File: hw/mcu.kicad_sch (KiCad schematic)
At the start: 38 parts, among them J6 SWD, U4 STM32G474CEU6, Y1 16MHz 9pF

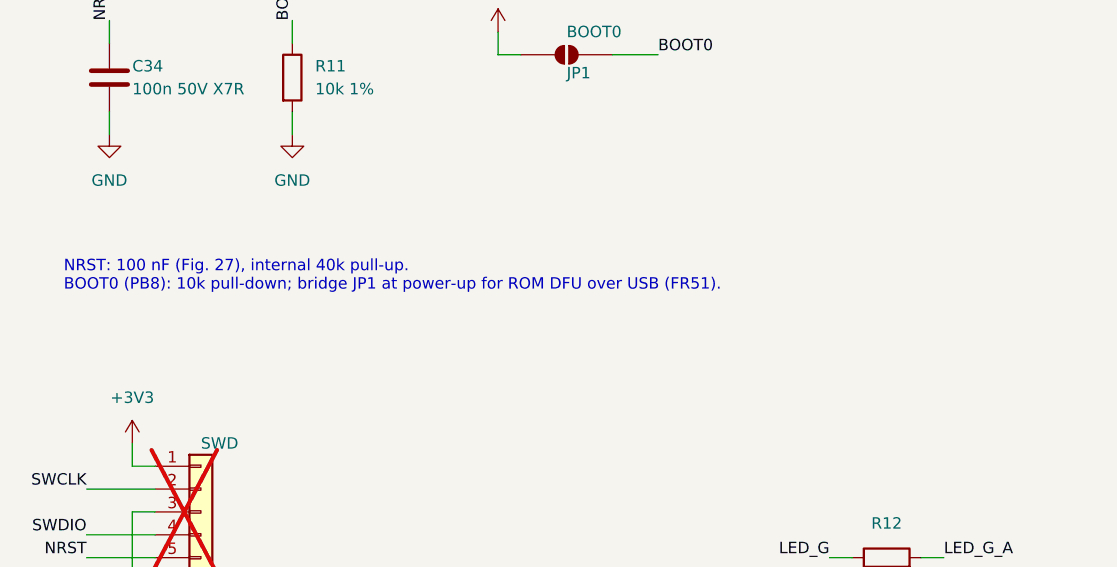
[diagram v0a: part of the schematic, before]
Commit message: Remove requirement IDs from schematic notes
Notes now state the reason in plain words so the schematic reads
without the requirements document.

Co-Authored-By: Claude Opus 5.5 <noreply@anthropic.com>
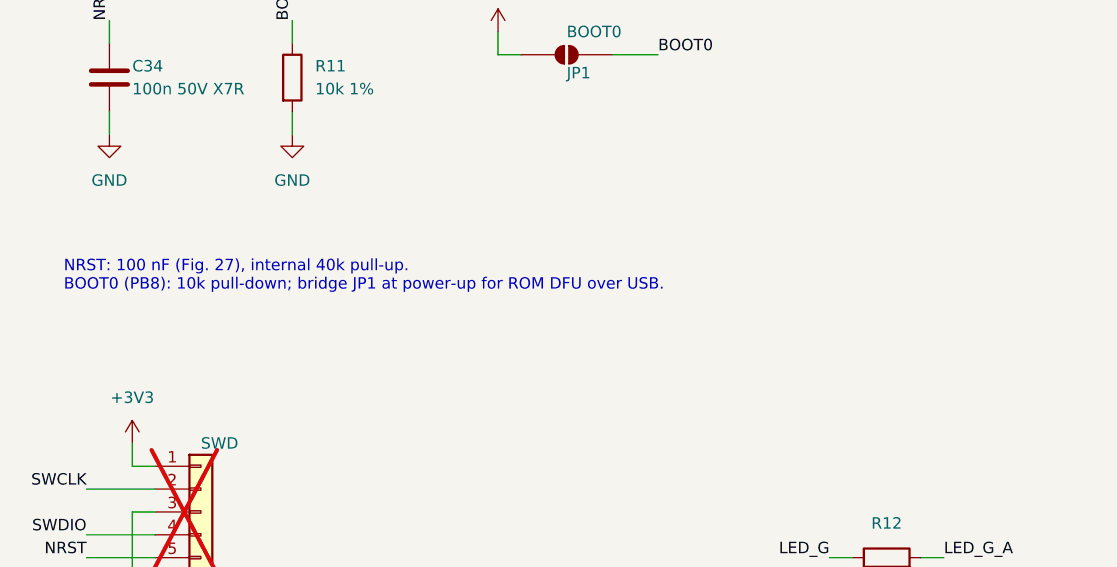
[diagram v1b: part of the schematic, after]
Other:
- note added: "NRST: 100 nF (Fig. 27), internal 40k pull-up. BOOT0 (PB8): 10k pull-down; bridge JP1 at power-up for ROM DFU over USB."
- note removed: "NRST: 100 nF (Fig. 27), internal 40k pull-up. BOOT0 (PB8): 10k pull-down; bridge JP1 at power-up for ROM DFU over USB (FR51)."
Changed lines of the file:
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@@
 		)
 	)
-	(text "NRST: 100 nF (Fig. 27), internal 40k pull-up.\nBOOT0 (PB8): 10k pull-down; bridge JP1 at power-up for ROM DFU over USB (FR51)."
+	(text "NRST: 100 nF (Fig. 27), internal 40k pull-up.\nBOOT0 (PB8): 10k pull-down; bridge JP1 at power-up for ROM DFU over USB."
 		(exclude_from_sim no)
 		(at 25.4 172.72 0.0000)

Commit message: Place the 45 x 45 mm two-sided board and review its risks
Ceramic-only bulk caps, per-phase caps under each FET pair, one FET row,
corner M3 holes, USB-C and CAN on the motor side, XT30s closer together.
Encoder clearance 10 mm, 10 A RMS rating with no heatsink. Placement
fixes from the risk review: BOOT0 pad away from VBUS, 3 mm clear around
the XT30 power joints, edge caps parallel to the edge. Specs, layout
check and risk review updated; fuse and regen clamp now required
off-board parts.

Co-Authored-By: Claude Opus 5.5 <noreply@anthropic.com>
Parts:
- removed TP1: TP_3V3, TestPoint:TestPoint_Pad_D1.0mm, symbol Connector:TestPoint
- removed TP2: TP_5V, TestPoint:TestPoint_Pad_D1.0mm, symbol Connector:TestPoint
- removed TP3: TP_VBUS, TestPoint:TestPoint_Pad_D1.0mm, symbol Connector:TestPoint
- removed TP5: TP_SOA, TestPoint:TestPoint_Pad_D1.0mm, symbol Connector:TestPoint
- removed TP6: TP_SOB, TestPoint:TestPoint_Pad_D1.0mm, symbol Connector:TestPoint
- removed TP7: TP_SOC, TestPoint:TestPoint_Pad_D1.0mm, symbol Connector:TestPoint
- removed TP8: TP_DRV_nFAULT, TestPoint:TestPoint_Pad_D1.0mm, symbol Connector:TestPoint

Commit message: Route the 6-layer board and finalize parts for ordering
The 45 x 45 mm board is fully routed on six layers (F / GND / SIG /
SIG / PWR / B, 2 oz outer, 1 oz inner): DRC 0 errors, 0 unconnected,
schematic parity 0. Four layers could not route the DRV-to-MCU links
without moving the power or input stage.

- Encoder shares the DRV8353's SPI3 bus, as on the PoC; PA5-PA7 are
  unused. R25 pulls DRV nSCS up, since the DRV's logic inputs have an
  internal pull-down. The SDO / MISO pin-type warning is an ERC
  exclusion with a note.
- MCU is now the STM32G473CEU6: the G474 without the unused HRTIM,
  checked pin for pin against both datasheets, in stock and cheaper.
- Male XT30PW-M power connectors, HCS1206 shunts, SWD pads at the
  board edge.
- Design doc and review notes updated for the new stack-up, shared
  bus and MCU.

Co-Authored-By: Claude Opus 5.5 <noreply@anthropic.com>
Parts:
- J6: footprint Connector_PinHeader_2.54mm:PinHeader_1x05_P2.54mm_Vertical -> foc_controller:SWD_Pads_1x05_P1.27mm_SMD
- U4: value STM32G474CEU6 -> STM32G473CEU6; symbol MCU_ST_STM32G4:STM32G474CEUx -> MCU_ST_STM32G4:STM32G473CEUx; LCSC C1235412 -> C1342773; MPN STM32G474CEU6 -> STM32G473CEU6
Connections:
- net ENC_MISO is gone; now on net DRV_SDO: U4.40 (PC11)
- net ENC_MOSI is gone; now on net DRV_SDI: U4.43 (PB5)
- net ENC_SCK is gone; now on net DRV_SCLK: U4.39 (PC10)
- net CAN_TX: now also U4.42 (PB4); no longer U4.38 (PA15)
- net DRV_EN: now also U4.29 (PC6); no longer U4.24 (PB11)
- net DRV_SCLK: no longer U4.13 (PA5)
- net DRV_SDI: no longer U4.15 (PA7)
- net DRV_SDO: no longer U4.14 (PA6)
- net DRV_nFAULT: now also U4.44 (PB6); no longer U4.22 (PB10)
- net DRV_nSCS: now also U4.38 (PA15); no longer U4.45 (PB7)
- net ENC_CS: now also U4.24 (PB11); no longer U4.25 (PB12)
- net INHA: now also U4.32 (PA10); no longer U4.30 (PA8)
- net INHC: now also U4.30 (PA8); no longer U4.32 (PA10)
- net INLA: now also U4.28 (PB15); no longer U4.26 (PB13)
- net INLC: now also U4.26 (PB13); no longer U4.28 (PB15)
- no-connect marks 8 -> 11
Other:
- note added: "J6: 1.27 mm SMD pads for debugging only, Nucleo ST-LINK CN4 order (VDD, SWCLK, GND, SWDIO, NRST). Not fitted: solder wires or a 1.27 mm header if needed."
- note removed: "J6: 2.54 mm pads for debugging only, Nucleo ST-LINK CN4 order (VDD, SWCLK, GND, SWDIO, NRST). Not fitted: hand-solder a header if needed."
- title: MCU STM32G474 -> MCU STM32G473
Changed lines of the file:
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@@
 	(paper "A3")
 	(title_block
-		(title "MCU STM32G474")
+		(title "MCU STM32G473")
 		(date "2026-10-19")
 		(rev "A")
@@
 		)
 	)
-	(text "J6: 2.54 mm pads for debugging only, Nucleo ST-LINK CN4 order\n(VDD, SWCLK, GND, SWDIO, NRST). Not fitted: hand-solder a header if needed."
+	(text "J6: 1.27 mm SMD pads for debugging only, Nucleo ST-LINK CN4 order\n(VDD, SWCLK, GND, SWDIO, NRST). Not fitted: solder wires or a 1.27 mm header if needed."
 		(exclude_from_sim no)
 		(at 25.4 218.44 0)
@@
 	)
 	(no_connect
-		(at 187.96 149.86)
-	)
-	(no_connect
-		(at 187.96 154.94)
-	)
-	(no_connect
 		(at 187.96 134.62)
 	)
 	(no_connect
-		(at 187.96 121.92)
-	)
-	(no_connect
 		(at 187.96 119.38)
 	)
@@
 	(wire
 		(pts
-			(xy 187.96 165.1) (xy 180.34 165.1)
-		)
-		(stroke
-			(width 0)
-			(type default)
-		)
-	)
-	(wire
-		(pts
 			(xy 113.03 220.98) (xy 110.49 220.98)
 		)
@@
 	(wire
 		(pts
-			(xy 223.52 119.38) (xy 231.14 119.38)
-		)
-		(stroke
-			(width 0)
-			(type default)
-		)
-	)
-	(wire
-		(pts
 			(xy 76.2 44.45) (xy 76.2 46.99)
 		)
@@
 	(wire
 		(pts
-			(xy 223.52 116.84) (xy 231.14 116.84)
-		)
-		(stroke
-			(width 0)
-			(type default)
-		)
-	)
-	(wire
-		(pts
-			(xy 187.96 170.18) (xy 180.34 170.18)
-		)
-		(stroke
-			(width 0)
-			(type default)
-		)
-	)
-	(wire
-		(pts
 			(xy 121.92 44.45) (xy 121.92 46.99)
 		)
@@
 	(wire
 		(pts
-			(xy 187.96 157.48) (xy 180.34 157.48)
-		)
-		(stroke
-			(width 0)
-			(type default)
-		)
-	)
-	(wire
-		(pts
 			(xy 365.76 46.99) (xy 365.76 44.45)
 		)
@@
 	(wire
 		(pts
-			(xy 223.52 114.3) (xy 231.14 114.3)
-		)
-		(stroke
-			(width 0)
-			(type default)
-		)
-	)
-	(wire
-		(pts
 			(xy 223.52 121.92) (xy 231.14 121.92)
 		)
@@
 		)
 	)
-	(hierarchical_label "INHC"
+	(hierarchical_label "INHA"
 		(shape output)
 		(at 231.14 127 0)
@@
 		)
 	)
-	(hierarchical_label "DRV_SDO"
-		(shape input)
-		(at 231.14 116.84 0)
-		(effects
-			(font
-				(size 1.27 1.27)
-			)
-			(justify left)
-		)
-	)
-	(hierarchical_label "INHA"
+	(hierarchical_label "INHC"
 		(shape output)
 		(at 231.14 121.92 0)
@@
 		)
 	)
-	(hierarchical_label "ENC_CS"
-		(shape output)
-		(at 180.34 170.18 180)
-		(effects
-			(font
-				(size 1.27 1.27)
-			)
-			(justify right)
-		)
-	)
-	(hierarchical_label "ENC_MOSI"
+	(hierarchical_label "DRV_SDI"
 		(shape output)
 		(at 180.34 152.4 180)
@@
 		)
 	)
-	(hierarchical_label "DRV_SCLK"
-		(shape output)
-		(at 231.14 114.3 0)
-		(effects
-			(font
-				(size 1.27 1.27)
-			)
-			(justify left)
-		)
-	)
-	(hierarchical_label "INLC"
+	(hierarchical_label "INLA"
 		(shape output)
 		(at 180.34 177.8 180)
@@
 		)
 	)
-	(hierarchical_label "ENC_SCK"
+	(hierarchical_label "DRV_SCLK"
 		(shape output)
 		(at 180.34 124.46 180)
@@
 		)
 	)
-	(hierarchical_label "DRV_nFAULT"
-		(shape input)
-		(at 180.34 165.1 180)
-		(effects
-			(font
-				(size 1.27 1.27)
-			)
-			(justify right)
-		)
-	)
-	(hierarchical_label "DRV_SDI"
-		(shape output)
-		(at 231.14 119.38 0)
-		(effects
-			(font
-				(size 1.27 1.27)
-			)
-			(justify left)
-		)
-	)
-	(hierarchical_label "DRV_EN"
+	(hierarchical_label "ENC_CS"
 		(shape output)
 		(at 180.34 167.64 180)
@@
 		)
 	)
-	(hierarchical_label "CAN_TX"
+	(hierarchical_label "DRV_nSCS"
 		(shape output)
 		(at 231.14 139.7 0)
@@
 		)
 	)
-	(hierarchical_label "DRV_nSCS"
-		(shape output)
-		(at 180.34 157.48 180)
-		(effects
-			(font
-				(size 1.27 1.27)
-			)
-			(justify right)
-		)
-	)
 	(hierarchical_label "CAN_STB"
 		(shape output)
@@
 		)
 	)
-	(hierarchical_label "INLA"
+	(hierarchical_label "INLC"
 		(shape output)
 		(at 180.34 172.72 180)
@@
 		)
 	)
-	(hierarchical_label "ENC_MISO"
+	(hierarchical_label "DRV_SDO"
 		(shape input)
 		(at 180.34 127 180)
@@
 			)
 		)
-		(property "Footprint" "Connector_PinHeader_2.54mm:PinHeader_1x05_P2.54mm_Vertical"
+		(property "Footprint" "foc_controller:SWD_Pads_1x05_P1.27mm_SMD"
 			(at 40.64 200.66 0)
 			(hide yes)
@@
 	)
 	(symbol
-		(lib_id "MCU_ST_STM32G4:STM32G474CEUx")
+		(lib_id "MCU_ST_STM32G4:STM32G473CEUx")
 		(at 205.74 139.7 0)
 		(unit 1)
@@
 			)
 		)
-		(property "Value" "STM32G474CEU6"
+		(property "Value" "STM32G473CEU6"
 			(at 213.36 184.15 0)
 			(show_name no)
@@
 			)
 		)
-		(property "Datasheet" "https://www.st.com/resource/en/datasheet/stm32g474ce.pdf"
+		(property "Datasheet" "https://www.st.com/resource/en/datasheet/stm32g473ce.pdf"
 			(at 205.74 139.7 0)
 			(hide yes)
@@
 			)
 		)
-		(property "LCSC" "C1235412"
+		(property "LCSC" "C1342773"
 			(at 208.28 144.7799 0)
 			(hide yes)
@@
 			)
 		)
-		(property "MPN" "STM32G474CEU6"
+		(property "MPN" "STM32G473CEU6"
 			(at 208.28 144.7799 0)
 			(hide yes)
@@
 		)
 	)
+	(wire
+		(pts
+			(xy 180.34 149.86) (xy 187.96 149.86)
+		)
+		(stroke
+			(width 0)
+			(type default)
+		)
+	)
+	(hierarchical_label "CAN_TX"
+		(shape output)
+		(at 180.34 149.86 180)
+		(effects
+			(font
+				(size 1.27 1.27)
+			)
+			(justify right)
+		)
+	)
+	(wire
+		(pts
+			(xy 180.34 154.94) (xy 187.96 154.94)
+		)
+		(stroke
+			(width 0)
+			(type default)
+		)
+	)
+	(hierarchical_label "DRV_nFAULT"
+		(shape input)
+		(at 180.34 154.94 180)
+		(effects
+			(font
+				(size 1.27 1.27)
+			)
+			(justify right)
+		)
+	)
+	(no_connect
+		(at 187.96 157.48)
+	)
+	(no_connect
+		(at 187.96 165.1)
+	)
+	(wire
+		(pts
+			(xy 187.96 121.92) (xy 180.34 121.92)
+		)
+		(stroke
+			(width 0)
+			(type default)
+		)
+	)
+	(hierarchical_label "DRV_EN"
+		(shape output)
+		(at 180.34 121.92 180)
+		(effects
+			(font
+				(size 1.27 1.27)
+			)
+			(justify right)
+		)
+	)
+	(no_connect
+		(at 187.96 170.18)
+	)
+	(no_connect
+		(at 223.52 114.3)
+	)
+	(no_connect
+		(at 223.52 116.84)
+	)
+	(no_connect
+		(at 223.52 119.38)
+	)
 	(sheet_instances

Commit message: Rename the GND test pad and keep silkscreen labels as text
TP4 is the only test pad left, so it becomes TP1 in the schematic,
board and docs.

The motor, SWD and CAN labels (A, B, C, DBUG, CAN1, CAN2) had been set
by renaming the reference designators on the board. That broke
schematic parity, and it would have dropped J7 and J8 from JLC
assembly, because the BOM lists them by their schematic references.
J3-J8 keep their references, hidden on silk, and each label is now a
text item on its footprint with the same position, size and layer.
The plotted silkscreen is identical to before.

Co-Authored-By: Claude Opus 5.5 <noreply@anthropic.com>
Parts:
- renumbered TP4 to TP1
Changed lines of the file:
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@@
 		(in_pos_files yes)
 		(dnp no)
-		(property "Reference" "TP4"
+		(property "Reference" "TP1"
 			(at 342.9 206.5 0)
 			(show_name no)
@@
 			(project "foc_controller"
 				(path "/dc3b1c6f-161a-46e4-9985-32c8fd205458/65a7b652-5191-47ae-a7b2-084cabfd7ef7"
-					(reference "TP4")
+					(reference "TP1")
 					(unit 1)
 				)
